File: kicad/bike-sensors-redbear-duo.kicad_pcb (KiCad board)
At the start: 2 copper layers, 38.1 x 45.7 mm, 13 parts, among them Q4 P_Channel_MOSFET, U2 Redbear_Duo, U3 GP2Y10_Dust_Particulate, U5 MQ-7_Carbon_Monoxide

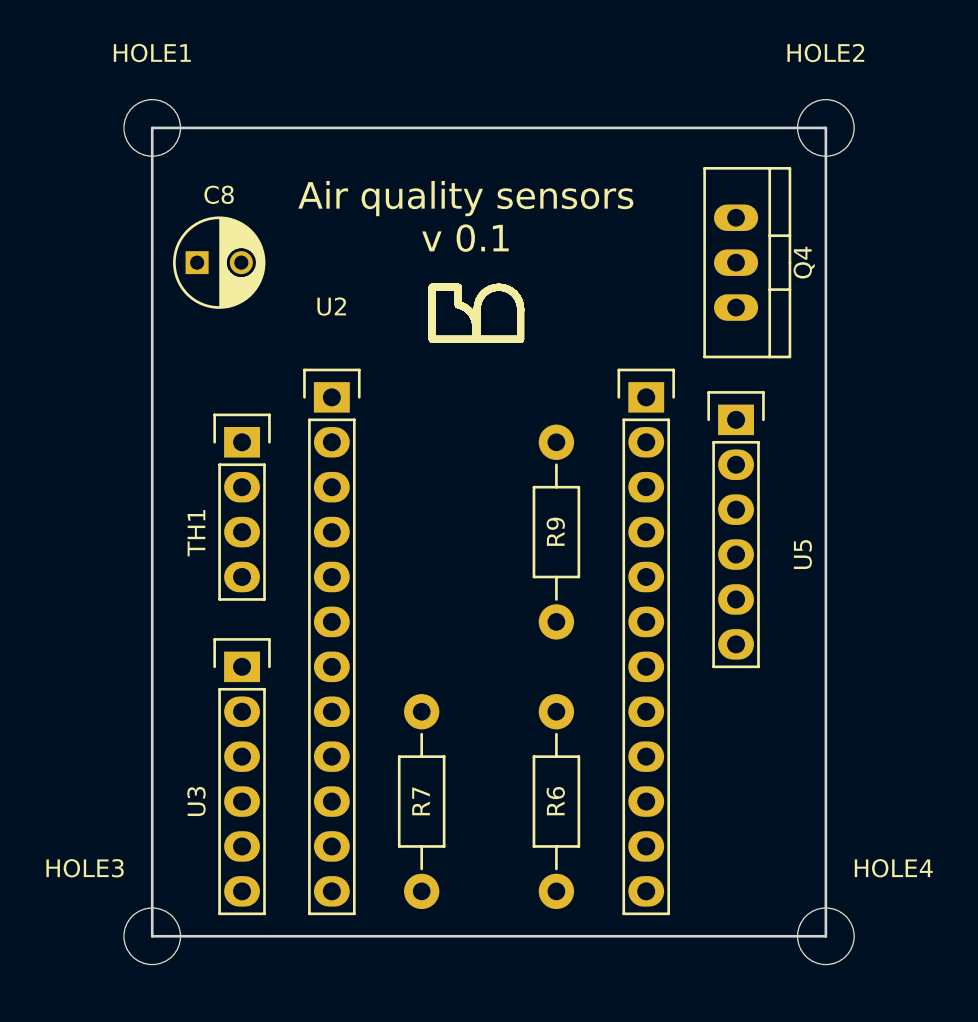
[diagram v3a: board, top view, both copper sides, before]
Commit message: Manually routed tracks.
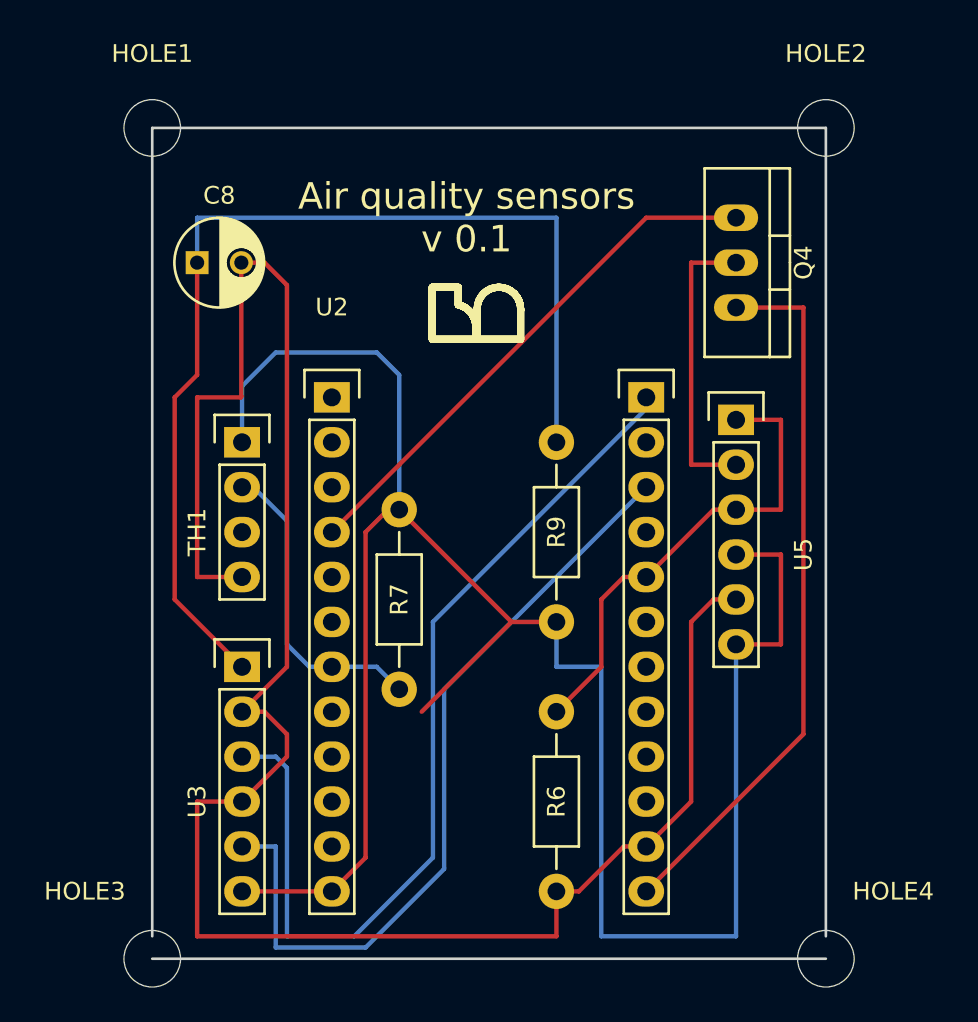
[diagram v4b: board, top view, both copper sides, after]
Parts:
- moved R7 11.5 mm to (166.4, 85.1)
- moved HOLE3 1.27 mm to (152.4, 110.5)
- moved HOLE4 1.27 mm to (190.5, 110.5)
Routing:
- net Net-(R7-Pad1): track 0.00 -> 122.9 mm
- net GND: track 0.00 -> 115.0 mm
- net Net-(C8-Pad1): track 0.00 -> 60.5 mm
- net Net-(U2-Pad24): track 0.00 -> 53.5 mm
- net Net-(U2-Pad22): track 0.00 -> 45.3 mm
- net Net-(Q4-Pad3): track 0.00 -> 40.5 mm
- net Net-(Q4-Pad1): track 0.00 -> 30.2 mm
- net Net-(R6-Pad1): track 0.00 -> 27.3 mm
- net Net-(R7-Pad2): track 0.00 -> 17.7 mm
- net Net-(Q4-Pad2): track 0.00 -> 16.5 mm
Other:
- board size 38.1 x 45.7 mm -> 38.1 x 47 mm
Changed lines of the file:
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@@
   (general
     (links 24)
-    (no_connects 24)
-    (area 152.324999 63.424999 190.575001 109.295001)
+    (no_connects 0)
+    (area 142.717857 58.125 200.182143 114.445)
     (thickness 1.6)
     (drawings 227)
-    (tracks 0)
+    (tracks 90)
     (zones 0)
     (modules 13)
@@
   )
   (module Resistors_ThroughHole:Resistor_Horizontal_RM10mm (layer F.Cu)
-    (at 167.64 96.52 270)
+    (at 166.37 85.09 270)
     (descr "Resistor, Axial,  RM 10mm, 1/3W")
     (tags "Resistor Axial RM 10mm 1/3W")
@@
   )
   (module Mounting_Holes:MountingHole_3.2mm_M3 (layer F.Cu)
-    (at 190.5 109.22)
+    (at 190.5 110.49)
     (descr "Mounting Hole 3.2mm, no annular, M3")
     (tags "mounting hole 3.2mm no annular m3")
@@
   )
   (module Mounting_Holes:MountingHole_3.2mm_M3 (layer F.Cu)
-    (at 152.4 109.22)
+    (at 152.4 110.49)
     (descr "Mounting Hole 3.2mm, no annular, M3")
     (tags "mounting hole 3.2mm no annular m3")
@@
   )
   (gr_line (start 190.5 109.22) (end 190.5 63.5) (angle 90) (layer Edge.Cuts) (width 0.15))
-  (gr_line (start 152.4 109.22) (end 190.5 109.22) (angle 90) (layer Edge.Cuts) (width 0.15))
+  (gr_line (start 152.4 110.49) (end 190.5 110.49) (angle 90) (layer Edge.Cuts) (width 0.15))
   (gr_line (start 152.4 63.5) (end 152.4 109.22) (angle 90) (layer Edge.Cuts) (width 0.15))
   (gr_line (start 190.5 63.5) (end 152.4 63.5) (angle 90) (layer Edge.Cuts) (width 0.15))
+  (segment (start 154.94 71.12) (end 154.94 68.58) (width 0.25) (layer B.Cu) (net 1))
+  (segment (start 175.26 68.58) (end 175.26 81.28) (width 0.25) (layer B.Cu) (net 1))
+  (segment (start 154.94 68.58) (end 175.26 68.58) (width 0.25) (layer B.Cu) (net 1))
+  (segment (start 154.94 71.12) (end 154.94 77.47) (width 0.25) (layer F.Cu) (net 1))
+  (segment (start 153.67 90.17) (end 157.48 93.98) (width 0.25) (layer F.Cu) (net 1))
+  (segment (start 153.67 78.74) (end 153.67 90.17) (width 0.25) (layer F.Cu) (net 1))
+  (segment (start 154.94 77.47) (end 153.67 78.74) (width 0.25) (layer F.Cu) (net 1))
+  (segment (start 157.44 71.12) (end 157.44 78.7) (width 0.25) (layer F.Cu) (net 2))
+  (segment (start 154.94 88.9) (end 157.48 88.9) (width 0.25) (layer F.Cu) (net 2))
+  (segment (start 154.94 78.74) (end 154.94 88.9) (width 0.25) (layer F.Cu) (net 2))
+  (segment (start 157.4 78.74) (end 154.94 78.74) (width 0.25) (layer F.Cu) (net 2))
+  (segment (start 157.44 78.7) (end 157.4 78.74) (width 0.25) (layer F.Cu) (net 2))
+  (segment (start 175.26 106.68) (end 175.26 109.22) (width 0.25) (layer F.Cu) (net 2))
+  (segment (start 154.94 101.6) (end 157.48 101.6) (width 0.25) (layer F.Cu) (net 2))
+  (segment (start 154.94 109.22) (end 154.94 101.6) (width 0.25) (layer F.Cu) (net 2))
+  (segment (start 175.26 109.22) (end 154.94 109.22) (width 0.25) (layer F.Cu) (net 2))
+  (segment (start 157.48 96.52) (end 158.75 96.52) (width 0.25) (layer F.Cu) (net 2))
+  (segment (start 158.75 96.52) (end 160.02 97.79) (width 0.25) (layer F.Cu) (net 2))
+  (segment (start 160.02 97.79) (end 160.02 99.06) (width 0.25) (layer F.Cu) (net 2))
+  (segment (start 160.02 99.06) (end 157.48 101.6) (width 0.25) (layer F.Cu) (net 2))
+  (segment (start 157.44 71.12) (end 158.75 71.12) (width 0.25) (layer F.Cu) (net 2))
+  (segment (start 160.02 93.98) (end 157.48 96.52) (width 0.25) (layer F.Cu) (net 2))
+  (segment (start 160.02 72.39) (end 160.02 93.98) (width 0.25) (layer F.Cu) (net 2))
+  (segment (start 158.75 71.12) (end 160.02 72.39) (width 0.25) (layer F.Cu) (net 2))
+  (segment (start 180.34 104.14) (end 179.07 104.14) (width 0.25) (layer F.Cu) (net 2))
+  (segment (start 176.53 106.68) (end 175.26 106.68) (width 0.25) (layer F.Cu) (net 2))
+  (segment (start 179.07 104.14) (end 176.53 106.68) (width 0.25) (layer F.Cu) (net 2))
+  (segment (start 185.42 90.17) (end 184.15 90.17) (width 0.25) (layer F.Cu) (net 2))
+  (segment (start 182.88 101.6) (end 180.34 104.14) (width 0.25) (layer F.Cu) (net 2))
+  (segment (start 182.88 91.44) (end 182.88 101.6) (width 0.25) (layer F.Cu) (net 2))
+  (segment (start 184.15 90.17) (end 182.88 91.44) (width 0.25) (layer F.Cu) (net 2))
+  (segment (start 185.42 71.12) (end 182.88 71.12) (width 0.25) (layer F.Cu) (net 3))
+  (segment (start 182.88 82.55) (end 185.42 82.55) (width 0.25) (layer F.Cu) (net 3))
+  (segment (start 182.88 71.12) (end 182.88 82.55) (width 0.25) (layer F.Cu) (net 3))
+  (segment (start 185.42 68.58) (end 180.34 68.58) (width 0.25) (layer F.Cu) (net 4))
+  (segment (start 180.34 68.58) (end 162.56 86.36) (width 0.25) (layer F.Cu) (net 4))
+  (segment (start 189.23 97.79) (end 180.34 106.68) (width 0.25) (layer F.Cu) (net 5))
+  (segment (start 189.23 73.66) (end 189.23 97.79) (width 0.25) (layer F.Cu) (net 5))
+  (segment (start 185.42 73.66) (end 189.23 73.66) (width 0.25) (layer F.Cu) (net 5))
+  (segment (start 180.34 88.9) (end 179.07 88.9) (width 0.25) (layer F.Cu) (net 6))
+  (segment (start 177.8 93.98) (end 175.26 96.52) (width 0.25) (layer F.Cu) (net 6))
+  (segment (start 177.8 90.17) (end 177.8 93.98) (width 0.25) (layer F.Cu) (net 6))
+  (segment (start 179.07 88.9) (end 177.8 90.17) (width 0.25) (layer F.Cu) (net 6))
+  (segment (start 185.42 85.09) (end 184.15 85.09) (width 0.25) (layer F.Cu) (net 6))
+  (segment (start 184.15 85.09) (end 180.34 88.9) (width 0.25) (layer F.Cu) (net 6))
+  (segment (start 185.42 80.01) (end 187.96 80.01) (width 0.25) (layer F.Cu) (net 6))
+  (segment (start 187.96 85.09) (end 185.42 85.09) (width 0.25) (layer F.Cu) (net 6))
+  (segment (start 187.96 80.01) (end 187.96 85.09) (width 0.25) (layer F.Cu) (net 6))
+  (segment (start 166.37 85.09) (end 166.37 77.47) (width 0.25) (layer B.Cu) (net 7) (status 400000))
+  (segment (start 157.48 78.105) (end 157.48 81.28) (width 0.25) (layer B.Cu) (net 7) (status 800000))
+  (segment (start 159.385 76.2) (end 157.48 78.105) (width 0.25) (layer B.Cu) (net 7))
+  (segment (start 165.1 76.2) (end 159.385 76.2) (width 0.25) (layer B.Cu) (net 7))
+  (segment (start 166.37 77.47) (end 165.1 76.2) (width 0.25) (layer B.Cu) (net 7))
+  (segment (start 166.37 85.09) (end 165.735 85.09) (width 0.25) (layer F.Cu) (net 7) (status C00000))
+  (segment (start 165.735 85.09) (end 164.465 86.36) (width 0.25) (layer F.Cu) (net 7) (status 400000))
+  (segment (start 164.465 104.775) (end 162.56 106.68) (width 0.25) (layer F.Cu) (net 7) (status 800000))
+  (segment (start 164.465 86.36) (end 164.465 104.775) (width 0.25) (layer F.Cu) (net 7))
+  (segment (start 175.26 91.44) (end 172.72 91.44) (width 0.25) (layer F.Cu) (net 7) (status 400000))
+  (segment (start 172.72 91.44) (end 166.37 85.09) (width 0.25) (layer F.Cu) (net 7) (status 800000))
+  (segment (start 175.26 91.44) (end 175.26 93.98) (width 0.25) (layer B.Cu) (net 7))
+  (segment (start 185.42 109.22) (end 185.42 92.71) (width 0.25) (layer B.Cu) (net 7))
+  (segment (start 177.8 109.22) (end 185.42 109.22) (width 0.25) (layer B.Cu) (net 7))
+  (segment (start 177.8 93.98) (end 177.8 109.22) (width 0.25) (layer B.Cu) (net 7))
+  (segment (start 175.26 93.98) (end 177.8 93.98) (width 0.25) (layer B.Cu) (net 7))
+  (segment (start 172.72 91.44) (end 167.64 96.52) (width 0.25) (layer F.Cu) (net 7))
+  (segment (start 157.48 106.68) (end 162.56 106.68) (width 0.25) (layer F.Cu) (net 7))
+  (segment (start 185.42 87.63) (end 187.96 87.63) (width 0.25) (layer F.Cu) (net 7))
+  (segment (start 187.96 87.63) (end 187.96 92.71) (width 0.25) (layer F.Cu) (net 7))
+  (segment (start 187.96 92.71) (end 185.42 92.71) (width 0.25) (layer F.Cu) (net 7))
+  (segment (start 162.56 93.98) (end 165.1 93.98) (width 0.25) (layer B.Cu) (net 8) (status 400000))
+  (segment (start 165.1 93.98) (end 166.37 95.25) (width 0.25) (layer B.Cu) (net 8) (status 800000))
+  (segment (start 157.48 83.82) (end 158.115 83.82) (width 0.25) (layer B.Cu) (net 8) (status C00000))
+  (segment (start 158.115 83.82) (end 160.02 85.725) (width 0.25) (layer B.Cu) (net 8) (status 400000))
+  (segment (start 160.02 85.725) (end 160.02 92.71) (width 0.25) (layer B.Cu) (net 8))
+  (segment (start 160.02 92.71) (end 161.29 93.98) (width 0.25) (layer B.Cu) (net 8))
+  (segment (start 161.29 93.98) (end 162.56 93.98) (width 0.25) (layer B.Cu) (net 8) (status 800000))
+  (segment (start 180.34 78.74) (end 180.34 79.375) (width 0.25) (layer B.Cu) (net 19) (status C00000))
+  (segment (start 180.34 79.375) (end 168.275 91.44) (width 0.25) (layer B.Cu) (net 19) (status 400000))
+  (segment (start 168.275 91.44) (end 168.275 104.775) (width 0.25) (layer B.Cu) (net 19))
+  (segment (start 168.275 104.775) (end 163.83 109.22) (width 0.25) (layer B.Cu) (net 19))
+  (segment (start 163.83 109.22) (end 160.02 109.22) (width 0.25) (layer B.Cu) (net 19))
+  (segment (start 160.02 109.22) (end 160.02 99.695) (width 0.25) (layer B.Cu) (net 19))
+  (segment (start 160.02 99.695) (end 159.385 99.06) (width 0.25) (layer B.Cu) (net 19))
+  (segment (start 159.385 99.06) (end 157.48 99.06) (width 0.25) (layer B.Cu) (net 19) (status 800000))
+  (segment (start 180.34 83.82) (end 168.91 95.25) (width 0.25) (layer B.Cu) (net 20) (status 400000))
+  (segment (start 159.385 104.14) (end 157.48 104.14) (width 0.25) (layer B.Cu) (net 20) (status 800000))
+  (segment (start 159.385 109.855) (end 159.385 104.14) (width 0.25) (layer B.Cu) (net 20))
+  (segment (start 164.465 109.855) (end 159.385 109.855) (width 0.25) (layer B.Cu) (net 20))
+  (segment (start 168.91 105.41) (end 164.465 109.855) (width 0.25) (layer B.Cu) (net 20))
+  (segment (start 168.91 95.25) (end 168.91 105.41) (width 0.25) (layer B.Cu) (net 20))
 )

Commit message: Fixed the board edge on the bottom. Sent v0.1 off for manufacturing
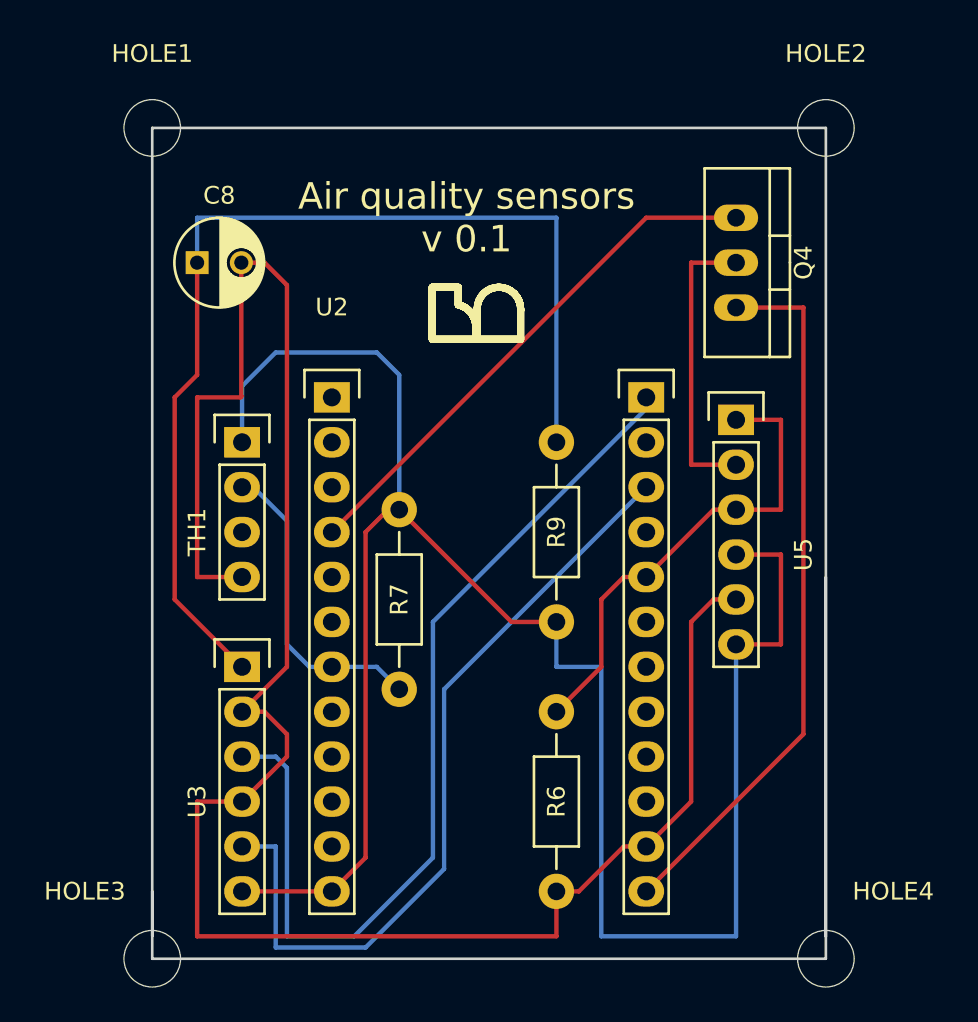
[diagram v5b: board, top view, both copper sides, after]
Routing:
- net Net-(R7-Pad1): track 122.9 -> 115.8 mm
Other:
- outline, holes or cut-outs redrawn
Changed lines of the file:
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@@
     (links 24)
     (no_connects 0)
-    (area 142.717857 58.125 200.182143 114.445)
+    (area 142.717857 58.125 200.182143 115.715)
     (thickness 1.6)
-    (drawings 227)
-    (tracks 90)
+    (drawings 230)
+    (tracks 89)
     (zones 0)
     (modules 13)
@@
     (pad 1 np_thru_hole circle (at 0 0) (size 3.2 3.2) (drill 3.2) (layers *.Cu *.Mask F.SilkS))
   )
+  (gr_line (start 152.4 110.49) (end 152.4 106.68) (angle 90) (layer Edge.Cuts) (width 0.15))
+  (gr_line (start 190.5 109.22) (end 190.5 88.9) (angle 90) (layer Edge.Cuts) (width 0.15))
+  (gr_line (start 190.5 110.49) (end 190.5 109.22) (angle 90) (layer Edge.Cuts) (width 0.15))
   (gr_line (start 173.140643 73.260868) (end 173.026455 73.05088) (layer F.SilkS) (width 0.4))
   (gr_line (start 173.026455 73.05088) (end 172.877062 72.869563) (layer F.SilkS) (width 0.4))
@@
   (segment (start 187.96 85.09) (end 185.42 85.09) (width 0.25) (layer F.Cu) (net 6))
   (segment (start 187.96 80.01) (end 187.96 85.09) (width 0.25) (layer F.Cu) (net 6))
-  (segment (start 166.37 85.09) (end 166.37 77.47) (width 0.25) (layer B.Cu) (net 7) (status 400000))
-  (segment (start 157.48 78.105) (end 157.48 81.28) (width 0.25) (layer B.Cu) (net 7) (status 800000))
+  (segment (start 166.37 85.09) (end 166.37 77.47) (width 0.25) (layer B.Cu) (net 7))
+  (segment (start 157.48 78.105) (end 157.48 81.28) (width 0.25) (layer B.Cu) (net 7))
   (segment (start 159.385 76.2) (end 157.48 78.105) (width 0.25) (layer B.Cu) (net 7))
   (segment (start 165.1 76.2) (end 159.385 76.2) (width 0.25) (layer B.Cu) (net 7))
   (segment (start 166.37 77.47) (end 165.1 76.2) (width 0.25) (layer B.Cu) (net 7))
-  (segment (start 166.37 85.09) (end 165.735 85.09) (width 0.25) (layer F.Cu) (net 7) (status C00000))
-  (segment (start 165.735 85.09) (end 164.465 86.36) (width 0.25) (layer F.Cu) (net 7) (status 400000))
-  (segment (start 164.465 104.775) (end 162.56 106.68) (width 0.25) (layer F.Cu) (net 7) (status 800000))
+  (segment (start 166.37 85.09) (end 165.735 85.09) (width 0.25) (layer F.Cu) (net 7))
+  (segment (start 165.735 85.09) (end 164.465 86.36) (width 0.25) (layer F.Cu) (net 7))
+  (segment (start 164.465 104.775) (end 162.56 106.68) (width 0.25) (layer F.Cu) (net 7))
   (segment (start 164.465 86.36) (end 164.465 104.775) (width 0.25) (layer F.Cu) (net 7))
-  (segment (start 175.26 91.44) (end 172.72 91.44) (width 0.25) (layer F.Cu) (net 7) (status 400000))
-  (segment (start 172.72 91.44) (end 166.37 85.09) (width 0.25) (layer F.Cu) (net 7) (status 800000))
+  (segment (start 175.26 91.44) (end 172.72 91.44) (width 0.25) (layer F.Cu) (net 7))
+  (segment (start 172.72 91.44) (end 166.37 85.09) (width 0.25) (layer F.Cu) (net 7))
   (segment (start 175.26 91.44) (end 175.26 93.98) (width 0.25) (layer B.Cu) (net 7))
   (segment (start 185.42 109.22) (end 185.42 92.71) (width 0.25) (layer B.Cu) (net 7))
@@
   (segment (start 177.8 93.98) (end 177.8 109.22) (width 0.25) (layer B.Cu) (net 7))
   (segment (start 175.26 93.98) (end 177.8 93.98) (width 0.25) (layer B.Cu) (net 7))
-  (segment (start 172.72 91.44) (end 167.64 96.52) (width 0.25) (layer F.Cu) (net 7))
   (segment (start 157.48 106.68) (end 162.56 106.68) (width 0.25) (layer F.Cu) (net 7))
   (segment (start 185.42 87.63) (end 187.96 87.63) (width 0.25) (layer F.Cu) (net 7))
   (segment (start 187.96 87.63) (end 187.96 92.71) (width 0.25) (layer F.Cu) (net 7))
   (segment (start 187.96 92.71) (end 185.42 92.71) (width 0.25) (layer F.Cu) (net 7))
-  (segment (start 162.56 93.98) (end 165.1 93.98) (width 0.25) (layer B.Cu) (net 8) (status 400000))
-  (segment (start 165.1 93.98) (end 166.37 95.25) (width 0.25) (layer B.Cu) (net 8) (status 800000))
-  (segment (start 157.48 83.82) (end 158.115 83.82) (width 0.25) (layer B.Cu) (net 8) (status C00000))
-  (segment (start 158.115 83.82) (end 160.02 85.725) (width 0.25) (layer B.Cu) (net 8) (status 400000))
+  (segment (start 162.56 93.98) (end 165.1 93.98) (width 0.25) (layer B.Cu) (net 8))
+  (segment (start 165.1 93.98) (end 166.37 95.25) (width 0.25) (layer B.Cu) (net 8))
+  (segment (start 157.48 83.82) (end 158.115 83.82) (width 0.25) (layer B.Cu) (net 8))
+  (segment (start 158.115 83.82) (end 160.02 85.725) (width 0.25) (layer B.Cu) (net 8))
   (segment (start 160.02 85.725) (end 160.02 92.71) (width 0.25) (layer B.Cu) (net 8))
   (segment (start 160.02 92.71) (end 161.29 93.98) (width 0.25) (layer B.Cu) (net 8))
-  (segment (start 161.29 93.98) (end 162.56 93.98) (width 0.25) (layer B.Cu) (net 8) (status 800000))
-  (segment (start 180.34 78.74) (end 180.34 79.375) (width 0.25) (layer B.Cu) (net 19) (status C00000))
-  (segment (start 180.34 79.375) (end 168.275 91.44) (width 0.25) (layer B.Cu) (net 19) (status 400000))
+  (segment (start 161.29 93.98) (end 162.56 93.98) (width 0.25) (layer B.Cu) (net 8))
+  (segment (start 180.34 78.74) (end 180.34 79.375) (width 0.25) (layer B.Cu) (net 19))
+  (segment (start 180.34 79.375) (end 168.275 91.44) (width 0.25) (layer B.Cu) (net 19))
   (segment (start 168.275 91.44) (end 168.275 104.775) (width 0.25) (layer B.Cu) (net 19))
   (segment (start 168.275 104.775) (end 163.83 109.22) (width 0.25) (layer B.Cu) (net 19))
@@
   (segment (start 160.02 109.22) (end 160.02 99.695) (width 0.25) (layer B.Cu) (net 19))
   (segment (start 160.02 99.695) (end 159.385 99.06) (width 0.25) (layer B.Cu) (net 19))
-  (segment (start 159.385 99.06) (end 157.48 99.06) (width 0.25) (layer B.Cu) (net 19) (status 800000))
-  (segment (start 180.34 83.82) (end 168.91 95.25) (width 0.25) (layer B.Cu) (net 20) (status 400000))
-  (segment (start 159.385 104.14) (end 157.48 104.14) (width 0.25) (layer B.Cu) (net 20) (status 800000))
+  (segment (start 159.385 99.06) (end 157.48 99.06) (width 0.25) (layer B.Cu) (net 19))
+  (segment (start 180.34 83.82) (end 168.91 95.25) (width 0.25) (layer B.Cu) (net 20))
+  (segment (start 159.385 104.14) (end 157.48 104.14) (width 0.25) (layer B.Cu) (net 20))
   (segment (start 159.385 109.855) (end 159.385 104.14) (width 0.25) (layer B.Cu) (net 20))
   (segment (start 164.465 109.855) (end 159.385 109.855) (width 0.25) (layer B.Cu) (net 20))
